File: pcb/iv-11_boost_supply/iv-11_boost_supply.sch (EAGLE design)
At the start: 4 parts

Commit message: Got all the parts in place, also found some more parts
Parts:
- added C2: 47uF, SparkFun-Passives:CAP_POLPTH1
- added C3: 100uF, SparkFun-Passives:CAP_POLPTH1
- added D1: 1N4004, adafruit:1N4004
- added D2: MBR160, adafruit:SCHOTTKY-DIODEDO201T15
- added D3: DIODE-ZENERPTH, SparkFun-DiscreteSemi:DIODE-ZENERPTH
- added IC1: LM555D, adafruit:LM555D
- added L1: 2200uH, SparkFun-Passives:INDUCTORRLB0912
- added M1: IRF540NPBF, boztalay:IRF540NPBF
- added R5: TRIMPOT, SparkFun-Electromechanical:TRIMPOT
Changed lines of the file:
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@@
 <layer number="54" name="bGND_GNDA" color="1" fill="9" visible="no" active="no"/>
 <layer number="56" name="wert" color="7" fill="1" visible="no" active="no"/>
+<layer number="57" name="tCAD" color="7" fill="1" visible="no" active="no"/>
 <layer number="90" name="Modules" color="5" fill="1" visible="yes" active="yes"/>
 <layer number="91" name="Nets" color="2" fill="1" visible="yes" active="yes"/>
@@
 <layer number="97" name="Info" color="7" fill="1" visible="yes" active="yes"/>
 <layer number="98" name="Guide" color="6" fill="1" visible="yes" active="yes"/>
+<layer number="99" name="SpiceOrder" color="7" fill="1" visible="yes" active="yes"/>
 <layer number="100" name="Muster" color="7" fill="1" visible="no" active="no"/>
 <layer number="101" name="Patch_Top" color="12" fill="4" visible="yes" active="yes"/>
@@
 <layer number="108" name="tplace-old" color="10" fill="1" visible="yes" active="yes"/>
 <layer number="109" name="ref-old" color="11" fill="1" visible="yes" active="yes"/>
+<layer number="110" name="fp0" color="7" fill="1" visible="no" active="yes"/>
+<layer number="111" name="LPC17xx" color="7" fill="1" visible="no" active="yes"/>
+<layer number="112" name="tSilk" color="7" fill="1" visible="no" active="yes"/>
+<layer number="113" name="IDFDebug" color="4" fill="1" visible="no" active="yes"/>
 <layer number="116" name="Patch_BOT" color="9" fill="4" visible="yes" active="yes"/>
 <layer number="121" name="_tsilk" color="7" fill="1" visible="yes" active="yes"/>
 <layer number="122" name="_bsilk" color="7" fill="1" visible="yes" active="yes"/>
+<layer number="123" name="tTestmark" color="7" fill="1" visible="no" active="yes"/>
+<layer number="124" name="bTestmark" color="7" fill="1" visible="no" active="yes"/>
 <layer number="125" name="_tNames" color="7" fill="1" visible="yes" active="yes"/>
+<layer number="126" name="_bNames" color="7" fill="1" visible="no" active="yes"/>
+<layer number="127" name="_tValues" color="7" fill="1" visible="no" active="yes"/>
+<layer number="128" name="_bValues" color="7" fill="1" visible="no" active="yes"/>
+<layer number="131" name="tAdjust" color="7" fill="1" visible="no" active="yes"/>
+<layer number="132" name="bAdjust" color="7" fill="1" visible="no" active="yes"/>
 <layer number="144" name="Drill_legend" color="7" fill="1" visible="yes" active="yes"/>
+<layer number="150" name="Notes" color="7" fill="1" visible="no" active="yes"/>
 <layer number="151" name="HeatSink" color="7" fill="1" visible="yes" active="yes"/>
+<layer number="152" name="_bDocu" color="7" fill="1" visible="no" active="yes"/>
+<layer number="153" name="FabDoc1" color="7" fill="1" visible="no" active="yes"/>
+<layer number="154" name="FabDoc2" color="7" fill="1" visible="no" active="yes"/>
+<layer number="155" name="FabDoc3" color="7" fill="1" visible="no" active="yes"/>
 <layer number="199" name="Contour" color="7" fill="1" visible="yes" active="yes"/>
 <layer number="200" name="200bmp" color="1" fill="10" visible="yes" active="yes"/>
@@
 <layer number="223" name="223bmp" color="24" fill="1" visible="no" active="no"/>
 <layer number="224" name="224bmp" color="25" fill="1" visible="no" active="no"/>
+<layer number="248" name="Housing" color="7" fill="1" visible="no" active="yes"/>
+<layer number="249" name="Edge" color="7" fill="1" visible="no" active="yes"/>
 <layer number="250" name="Descript" color="3" fill="1" visible="no" active="no"/>
 <layer number="251" name="SMDround" color="12" fill="11" visible="no" active="no"/>
@@
 <part name="R3" library="SparkFun-Passives" deviceset="RESISTOR" device="1206" value="10k"/>
 <part name="C1" library="SparkFun-Passives" deviceset="CAP" device="1206" value="10nF"/>
+<part name="C2" library="SparkFun-Passives" deviceset="CAP_POL" device="PTH1" value="47uF"/>
+<part name="C3" library="SparkFun-Passives" deviceset="CAP_POL" device="PTH1" value="100uF"/>
+<part name="R5" library="SparkFun-Electromechanical" deviceset="TRIMPOT" device=""/>
+<part name="D1" library="adafruit" deviceset="1N4004" device=""/>
+<part name="IC1" library="adafruit" deviceset="*555" device="D" technology="LM"/>
+<part name="M1" library="boztalay" deviceset="IRF540NPBF" device=""/>
+<part name="L1" library="SparkFun-Passives" deviceset="INDUCTOR" device="RLB0912" value="2200uH"/>
+<part name="D2" library="adafruit" deviceset="SCHOTTKY-DIODE" device="DO201T15" value="MBR160"/>
+<part name="D3" library="SparkFun-DiscreteSemi" deviceset="DIODE-ZENER" device="PTH"/>
 </parts>
 <sheets>
@@
 <instance part="R3" gate="G$1" x="88.9" y="66.04"/>
 <instance part="C1" gate="G$1" x="88.9" y="48.26"/>
+<instance part="C2" gate="G$1" x="99.06" y="78.74"/>
+<instance part="C3" gate="G$1" x="109.22" y="63.5"/>
+<instance part="R5" gate="R?" x="38.1" y="78.74"/>
+<instance part="D1" gate="1" x="66.04" y="81.28"/>
+<instance part="IC1" gate="A" x="35.56" y="55.88"/>
+<instance part="M1" gate="G$1" x="71.12" y="38.1"/>
+<instance part="L1" gate="G$1" x="114.3" y="43.18"/>
+<instance part="D2" gate="G$1" x="134.62" y="81.28"/>
+<instance part="D3" gate="G$1" x="134.62" y="66.04"/>
 </instances>
 <busses>

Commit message: Made a fuse part, got the rest of the parts in place
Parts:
- added F1: 2A/32V, boztalay:1AG-1/4X5/8-FUSE
- added JP1: (no value), SparkFun-Connectors:M05LOCK
- D3: value DIODE-ZENERPTH -> 1N5264B
- R5: value TRIMPOT -> 10k
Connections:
- new net BST: JP1.5
- new net FBK: JP1.4
- new net GND: JP1.2
- new net PWM: JP1.3
- new net VCC: JP1.1
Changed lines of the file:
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@@
 <part name="C2" library="SparkFun-Passives" deviceset="CAP_POL" device="PTH1" value="47uF"/>
 <part name="C3" library="SparkFun-Passives" deviceset="CAP_POL" device="PTH1" value="100uF"/>
-<part name="R5" library="SparkFun-Electromechanical" deviceset="TRIMPOT" device=""/>
+<part name="R5" library="SparkFun-Electromechanical" deviceset="TRIMPOT" device="" value="10k"/>
 <part name="D1" library="adafruit" deviceset="1N4004" device=""/>
 <part name="IC1" library="adafruit" deviceset="*555" device="D" technology="LM"/>
@@
 <part name="L1" library="SparkFun-Passives" deviceset="INDUCTOR" device="RLB0912" value="2200uH"/>
 <part name="D2" library="adafruit" deviceset="SCHOTTKY-DIODE" device="DO201T15" value="MBR160"/>
-<part name="D3" library="SparkFun-DiscreteSemi" deviceset="DIODE-ZENER" device="PTH"/>
+<part name="D3" library="SparkFun-DiscreteSemi" deviceset="DIODE-ZENER" device="PTH" value="1N5264B"/>
+<part name="JP1" library="SparkFun-Connectors" deviceset="M05" device="LOCK"/>
+<part name="F1" library="boztalay" deviceset="1AG-1/4X5/8-FUSE" device="" value="2A/32V"/>
+<part name="SUPPLY1" library="SparkFun-Aesthetics" deviceset="VCC" device=""/>
+<part name="GND1" library="SparkFun-Aesthetics" deviceset="GND" device=""/>
 </parts>
 <sheets>
@@
 <instance part="D2" gate="G$1" x="134.62" y="81.28"/>
 <instance part="D3" gate="G$1" x="134.62" y="66.04"/>
+<instance part="JP1" gate="G$1" x="-12.7" y="73.66"/>
+<instance part="F1" gate="G$1" x="78.74" y="25.4"/>
+<instance part="SUPPLY1" gate="G$1" x="0" y="68.58" rot="R180"/>
+<instance part="GND1" gate="1" x="5.08" y="66.04"/>
 </instances>
 <busses>
 </busses>
 <nets>
+<net name="VCC" class="0">
+<segment>
+<pinref part="JP1" gate="G$1" pin="1"/>
+<wire x1="-5.08" y1="68.58" x2="0" y2="68.58" width="0.1524" layer="91"/>
+<pinref part="SUPPLY1" gate="G$1" pin="VCC"/>
+</segment>
+</net>
+<net name="GND" class="0">
+<segment>
+<pinref part="JP1" gate="G$1" pin="2"/>
+<pinref part="GND1" gate="1" pin="GND"/>
+<wire x1="-5.08" y1="71.12" x2="5.08" y2="71.12" width="0.1524" layer="91"/>
+<wire x1="5.08" y1="71.12" x2="5.08" y2="68.58" width="0.1524" layer="91"/>
+</segment>
+</net>
+<net name="PWM" class="0">
+<segment>
+<pinref part="JP1" gate="G$1" pin="3"/>
+<wire x1="-5.08" y1="73.66" x2="0" y2="73.66" width="0.1524" layer="91"/>
+<label x="0.508" y="72.898" size="1.524" layer="95"/>
+</segment>
+</net>
+<net name="FBK" class="0">
+<segment>
+<pinref part="JP1" gate="G$1" pin="4"/>
+<wire x1="-5.08" y1="76.2" x2="0" y2="76.2" width="0.1524" layer="91"/>
+<label x="0.508" y="75.438" size="1.524" layer="95"/>
+</segment>
+</net>
+<net name="BST" class="0">
+<segment>
+<pinref part="JP1" gate="G$1" pin="5"/>
+<wire x1="-5.08" y1="78.74" x2="0" y2="78.74" width="0.1524" layer="91"/>
+<label x="0.508" y="77.978" size="1.524" layer="95"/>
+</segment>
+</net>
 </nets>
 </sheet>

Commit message: Did most of the board layout, found more parts to order
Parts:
- added JP2: (no value), SparkFun-Connectors:M03LOCK
- added R4: 10k, SparkFun-Passives:RESISTOR1206
- added R6: 110k, SparkFun-Passives:RESISTOR1206
- D2: device adafruit:SCHOTTKY-DIODEDO201T15 -> adafruit:SCHOTTKY-DIODEDO35-7
- M1: value IRF540NPBF -> IRF540
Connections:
- removed net PWM: JP1.3
- new net 555_CAP: C1.1, D1.C, IC1.THR, IC1.TR, R2.1
- new net 555_CTL: D1.A, IC1.DIS, R5.WIPER
- new net 555_PWM: IC1.Q, JP2.3
- new net EXT_PWM: JP1.3, JP2.1
- new net N$1: R1.1, R5.CCW
- new net N$2: R2.2, R5.CW
- new net N$4: D2.A, L1.2, M1.D
- new net PWR_PWM: JP2.2, M1.G, R3.2
- new net VCC_PRC: C2.+, F1.1, IC1.R, IC1.V+, L1.1, R1.2
- net BST: now also C3.+, D2.C, D3.C, R6.1
- net FBK: now also R4.1, R6.2
- net GND: now also C1.2, C2.-, C3.-, D3.A, IC1.GND, M1.S, R3.1, R4.2
- net VCC: now also F1.2
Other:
- moved on the sheet: C1, C2, C3, D1, D2, D3, F1, IC1, JP1, L1, M1, R1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

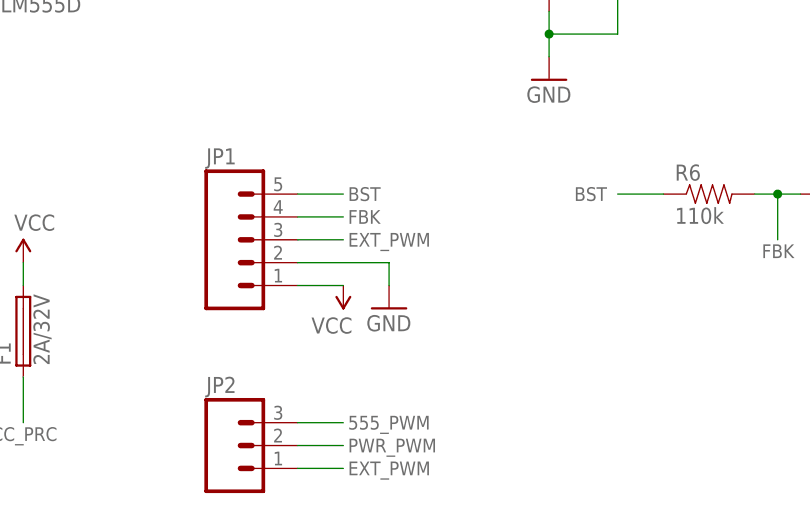
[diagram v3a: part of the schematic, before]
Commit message: Cleaned up the board layout, need the parts to test it out on paper
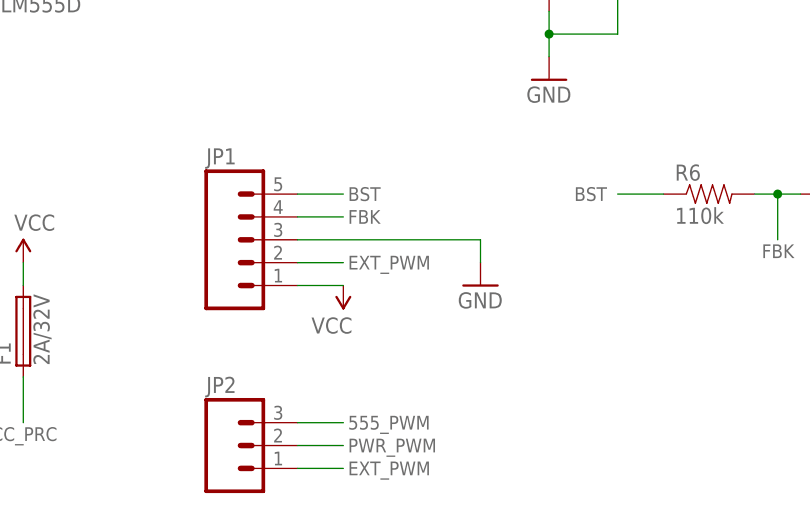
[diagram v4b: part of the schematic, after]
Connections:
- net EXT_PWM: now also JP1.2; no longer JP1.3
- net GND: now also JP1.3; no longer JP1.2
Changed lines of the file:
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@@
 <part name="F1" library="boztalay" deviceset="1AG-1/4X5/8-FUSE" device="" value="2A/32V"/>
 <part name="SUPPLY1" library="SparkFun-Aesthetics" deviceset="VCC" device=""/>
-<part name="GND1" library="SparkFun-Aesthetics" deviceset="GND" device=""/>
 <part name="GND2" library="SparkFun-Aesthetics" deviceset="GND" device=""/>
 <part name="GND3" library="SparkFun-Aesthetics" deviceset="GND" device=""/>
@@
 <part name="GND7" library="SparkFun-Aesthetics" deviceset="GND" device=""/>
 <part name="D2" library="adafruit" deviceset="SCHOTTKY-DIODE" device="DO35-7" value="MBR160"/>
+<part name="GND1" library="SparkFun-Aesthetics" deviceset="GND" device=""/>
 </parts>
 <sheets>
@@
 <instance part="F1" gate="G$1" x="38.1" y="12.7" rot="R90"/>
 <instance part="SUPPLY1" gate="G$1" x="73.66" y="17.78" rot="R180"/>
-<instance part="GND1" gate="1" x="78.74" y="15.24"/>
 <instance part="GND2" gate="1" x="30.48" y="48.26"/>
 <instance part="GND3" gate="1" x="-7.62" y="20.32"/>
@@
 <instance part="GND7" gate="1" x="137.16" y="22.86"/>
 <instance part="D2" gate="G$1" x="121.92" y="71.12"/>
+<instance part="GND1" gate="1" x="88.9" y="17.78"/>
 </instances>
 <busses>
@@
 </net>
 <net name="GND" class="0">
-<segment>
-<pinref part="JP1" gate="G$1" pin="2"/>
-<pinref part="GND1" gate="1" pin="GND"/>
-<wire x1="68.58" y1="20.32" x2="78.74" y2="20.32" width="0.1524" layer="91"/>
-<wire x1="78.74" y1="20.32" x2="78.74" y2="17.78" width="0.1524" layer="91"/>
-</segment>
 <segment>
 <pinref part="IC1" gate="A" pin="GND"/>
@@
 <pinref part="GND7" gate="1" pin="GND"/>
 <wire x1="137.16" y1="27.94" x2="137.16" y2="25.4" width="0.1524" layer="91"/>
+</segment>
+<segment>
+<pinref part="JP1" gate="G$1" pin="3"/>
+<wire x1="68.58" y1="22.86" x2="88.9" y2="22.86" width="0.1524" layer="91"/>
+<wire x1="88.9" y1="22.86" x2="88.9" y2="20.32" width="0.1524" layer="91"/>
+<pinref part="GND1" gate="1" pin="GND"/>
 </segment>
 </net>
@@
 </segment>
 <segment>
-<pinref part="JP1" gate="G$1" pin="3"/>
-<wire x1="68.58" y1="22.86" x2="73.66" y2="22.86" width="0.1524" layer="91"/>
-<label x="74.168" y="22.098" size="1.524" layer="95"/>
-</segment>
-</net>
+<pinref part="JP1" gate="G$1" pin="2"/>
+<wire x1="68.58" y1="20.32" x2="73.66" y2="20.32" width="0.1524" layer="91"/>
+<label x="74.168" y="19.558" size="1.524" layer="95"/>
+</segment>
+</net>

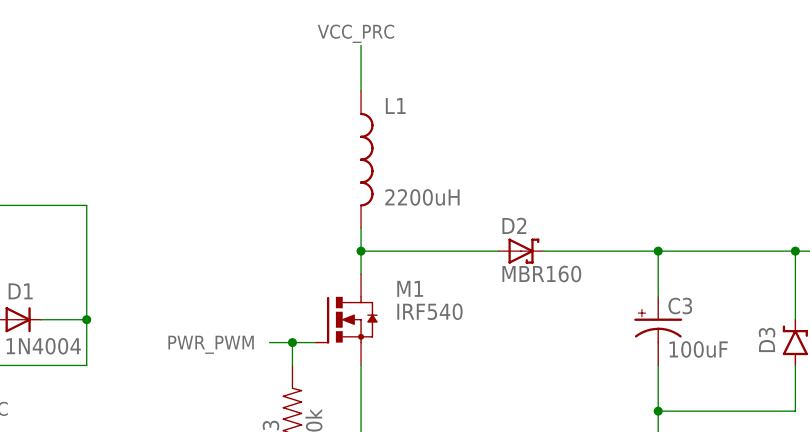
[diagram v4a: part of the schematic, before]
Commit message: Working on rev B of the boost supply board
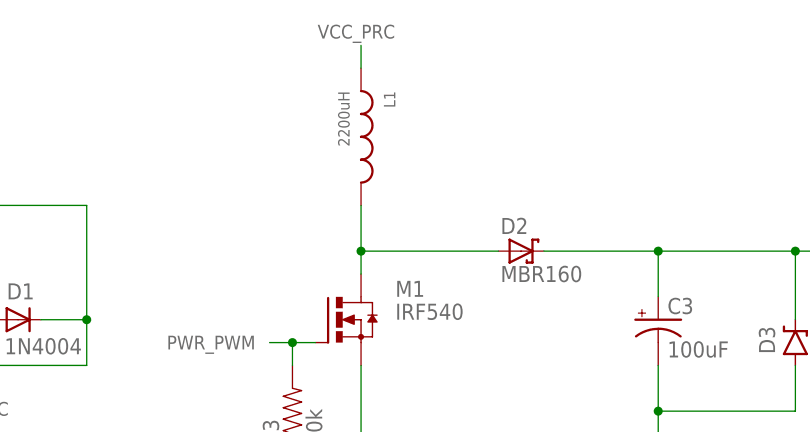
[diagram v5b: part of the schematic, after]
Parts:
- L1: device SparkFun-Passives:INDUCTORRLB0912 -> boztalay:INDUCTOR
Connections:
- net N$4: now also L1.B; no longer L1.2
- net VCC_PRC: now also L1.A; no longer L1.1
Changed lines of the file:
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@@
 <part name="IC1" library="adafruit" deviceset="*555" device="D" technology="LM"/>
 <part name="M1" library="boztalay" deviceset="IRF540NPBF" device="" value="IRF540"/>
-<part name="L1" library="SparkFun-Passives" deviceset="INDUCTOR" device="RLB0912" value="2200uH"/>
 <part name="D3" library="SparkFun-DiscreteSemi" deviceset="DIODE-ZENER" device="PTH" value="1N5264B"/>
 <part name="JP1" library="SparkFun-Connectors" deviceset="M05" device="LOCK"/>
@@
 <part name="D2" library="adafruit" deviceset="SCHOTTKY-DIODE" device="DO35-7" value="MBR160"/>
 <part name="GND1" library="SparkFun-Aesthetics" deviceset="GND" device=""/>
+<part name="L1" library="boztalay" deviceset="INDUCTOR" device="" value="2200uH"/>
 </parts>
 <sheets>
@@
 <instance part="IC1" gate="A" x="43.18" y="60.96"/>
 <instance part="M1" gate="G$1" x="101.6" y="63.5"/>
-<instance part="L1" gate="G$1" x="104.14" y="81.28"/>
 <instance part="D3" gate="G$1" x="152.4" y="60.96" smashed="yes" rot="R90">
 <attribute name="NAME" x="150.1394" y="59.69" size="1.778" layer="95" rot="R90"/>
@@
 <instance part="D2" gate="G$1" x="121.92" y="71.12"/>
 <instance part="GND1" gate="1" x="88.9" y="17.78"/>
+<instance part="L1" gate="G$1" x="104.14" y="83.82" rot="R270"/>
 </instances>
 <busses>
@@
 <net name="N$4" class="0">
 <segment>
-<pinref part="L1" gate="G$1" pin="2"/>
 <pinref part="M1" gate="G$1" pin="D"/>
-<wire x1="104.14" y1="73.66" x2="104.14" y2="71.12" width="0.1524" layer="91"/>
+<wire x1="104.14" y1="76.2" x2="104.14" y2="71.12" width="0.1524" layer="91"/>
 <wire x1="104.14" y1="71.12" x2="104.14" y2="68.58" width="0.1524" layer="91"/>
 <wire x1="104.14" y1="71.12" x2="119.38" y2="71.12" width="0.1524" layer="91"/>
 <junction x="104.14" y="71.12"/>
 <pinref part="D2" gate="G$1" pin="A"/>
+<pinref part="L1" gate="G$1" pin="B"/>
 </segment>
 </net>
@@
 </segment>
 <segment>
-<pinref part="L1" gate="G$1" pin="1"/>
-<wire x1="104.14" y1="93.98" x2="104.14" y2="88.9" width="0.1524" layer="91"/>
+<wire x1="104.14" y1="93.98" x2="104.14" y2="91.44" width="0.1524" layer="91"/>
 <label x="99.314" y="94.742" size="1.524" layer="95"/>
-</segment>
-<segment>
+<pinref part="L1" gate="G$1" pin="A"/>
+</segment>
+<segment>

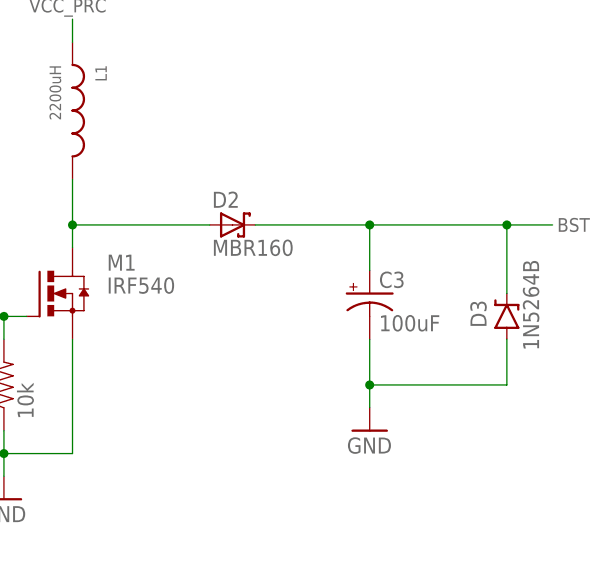
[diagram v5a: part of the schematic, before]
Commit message: Finished up rev B of the boost supply board, but the layout still needs to be tested
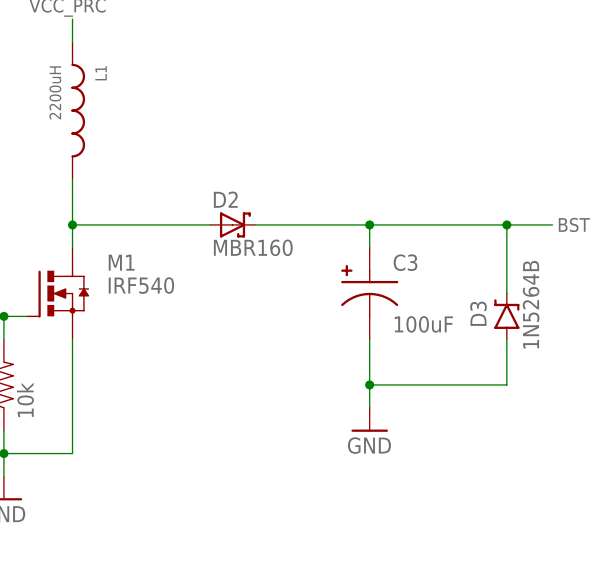
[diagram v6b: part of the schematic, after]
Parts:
- C3: device SparkFun-Passives:CAP_POLPTH1 -> boztalay:POLAR-CAP
- D2: device adafruit:SCHOTTKY-DIODEDO35-7 -> adafruit:SCHOTTKY-DIODEDO41
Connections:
- net BST: now also C3.A; no longer C3.+
- net GND: now also C3.B; no longer C3.-
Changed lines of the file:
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@@
 <part name="C1" library="SparkFun-Passives" deviceset="CAP" device="1206" value="10nF"/>
 <part name="C2" library="SparkFun-Passives" deviceset="CAP_POL" device="PTH1" value="47uF"/>
-<part name="C3" library="SparkFun-Passives" deviceset="CAP_POL" device="PTH1" value="100uF"/>
 <part name="R5" library="SparkFun-Electromechanical" deviceset="TRIMPOT" device="" value="10k"/>
 <part name="D1" library="adafruit" deviceset="1N4004" device=""/>
@@
 <part name="R6" library="SparkFun-Passives" deviceset="RESISTOR" device="1206" value="110k"/>
 <part name="GND7" library="SparkFun-Aesthetics" deviceset="GND" device=""/>
-<part name="D2" library="adafruit" deviceset="SCHOTTKY-DIODE" device="DO35-7" value="MBR160"/>
 <part name="GND1" library="SparkFun-Aesthetics" deviceset="GND" device=""/>
 <part name="L1" library="boztalay" deviceset="INDUCTOR" device="" value="2200uH"/>
+<part name="C3" library="boztalay" deviceset="POLAR-CAP" device="" value="100uF"/>
+<part name="D2" library="adafruit" deviceset="SCHOTTKY-DIODE" device="DO41" value="MBR160"/>
 </parts>
 <sheets>
@@
 <instance part="C1" gate="G$1" x="-7.62" y="27.94"/>
 <instance part="C2" gate="G$1" x="17.78" y="15.24"/>
-<instance part="C3" gate="G$1" x="137.16" y="63.5"/>
 <instance part="R5" gate="R?" x="-7.62" y="60.96" smashed="yes" rot="R270">
 <attribute name="NAME" x="-10.9474" y="57.912" size="1.778" layer="95" rot="R270"/>
@@
 <instance part="R6" gate="G$1" x="114.3" y="27.94"/>
 <instance part="GND7" gate="1" x="137.16" y="22.86"/>
-<instance part="D2" gate="G$1" x="121.92" y="71.12"/>
 <instance part="GND1" gate="1" x="88.9" y="17.78"/>
 <instance part="L1" gate="G$1" x="104.14" y="83.82" rot="R270"/>
+<instance part="C3" gate="G$1" x="137.16" y="63.5"/>
+<instance part="D2" gate="G$1" x="121.92" y="71.12"/>
 </instances>
 <busses>
@@
 </segment>
 <segment>
-<pinref part="C3" gate="G$1" pin="-"/>
 <pinref part="GND6" gate="1" pin="GND"/>
 <wire x1="137.16" y1="58.42" x2="137.16" y2="53.34" width="0.1524" layer="91"/>
@@
 <wire x1="152.4" y1="53.34" x2="137.16" y2="53.34" width="0.1524" layer="91"/>
 <junction x="137.16" y="53.34"/>
+<pinref part="C3" gate="G$1" pin="B"/>
 </segment>
 <segment>
@@
 </segment>
 <segment>
-<pinref part="C3" gate="G$1" pin="+"/>
 <wire x1="124.46" y1="71.12" x2="137.16" y2="71.12" width="0.1524" layer="91"/>
-<wire x1="137.16" y1="71.12" x2="137.16" y2="66.04" width="0.1524" layer="91"/>
+<wire x1="137.16" y1="71.12" x2="137.16" y2="68.58" width="0.1524" layer="91"/>
 <pinref part="D3" gate="G$1" pin="C"/>
 <wire x1="137.16" y1="71.12" x2="152.4" y2="71.12" width="0.1524" layer="91"/>
@@
 <junction x="152.4" y="71.12"/>
 <label x="157.988" y="70.358" size="1.524" layer="95"/>
+<pinref part="C3" gate="G$1" pin="A"/>
 <pinref part="D2" gate="G$1" pin="C"/>
 </segment>
@@
 <wire x1="104.14" y1="71.12" x2="119.38" y2="71.12" width="0.1524" layer="91"/>
 <junction x="104.14" y="71.12"/>
+<pinref part="L1" gate="G$1" pin="B"/>
 <pinref part="D2" gate="G$1" pin="A"/>
-<pinref part="L1" gate="G$1" pin="B"/>
-</segment>
-</net>
+</segment>
+</net>
